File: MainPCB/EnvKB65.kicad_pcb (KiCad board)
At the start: 2 copper layers, 320.8 x 99.3 mm, 151 parts, among them U0 Pico

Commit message: moved mount hole "H5" to the right by 40.5mm on all PCBs
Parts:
- moved H5 40.5 mm to (251.1, 183.5)

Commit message: replaced all mount holes with versions that have pads
I did this because the pcb can get scraped up if you take it apart a bunch of times to clean it, hopefully this mitigates that.
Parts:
- H0, H1, H2, H3, H4, H5: footprint MountingHole:MountingHole_2.2mm_M2 -> MountingHole:MountingHole_2.2mm_M2_Pad
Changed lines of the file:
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@@
     (add_net row4)
   )
+  (module MountingHole:MountingHole_2.2mm_M2_Pad (layer F.Cu)
+    (at 251.125 183.475)
+    (descr "Mounting Hole 2.2mm, M2")
+    (tags "mounting hole 2.2mm m2")
+    (attr virtual)
+    (fp_text reference H5 (at 0 -3.2) (layer Dwgs.User)
+      (effects (font (size 1 1) (thickness 0.15)))
+    )
+    (fp_text value MountingHole (at 0 3.2) (layer F.Fab)
+      (effects (font (size 1 1) (thickness 0.15)))
+    )
+    (fp_text user %R (at 0.3 0) (layer F.Fab)
+      (effects (font (size 1 1) (thickness 0.15)))
+    )
+    (fp_circle (center 0 0) (end 2.2 0) (layer Cmts.User) (width 0.15))
+    (fp_circle (center 0 0) (end 2.45 0) (layer F.CrtYd) (width 0.05))
+    (pad 1 thru_hole circle (at 0 0) (size 4.4 4.4) (drill 2.2) (layers *.Cu *.Mask))
+  )
+  (module MountingHole:MountingHole_2.2mm_M2_Pad (layer F.Cu)
+    (at 224.9 121.6)
+    (descr "Mounting Hole 2.2mm, M2")
+    (tags "mounting hole 2.2mm m2")
+    (attr virtual)
+    (fp_text reference H4 (at 0 -3.2) (layer Dwgs.User)
+      (effects (font (size 1 1) (thickness 0.15)))
+    )
+    (fp_text value MountingHole (at 0 3.2) (layer F.Fab)
+      (effects (font (size 1 1) (thickness 0.15)))
+    )
+    (fp_text user %R (at 0.3 0) (layer F.Fab)
+      (effects (font (size 1 1) (thickness 0.15)))
+    )
+    (fp_circle (center 0 0) (end 2.2 0) (layer Cmts.User) (width 0.15))
+    (fp_circle (center 0 0) (end 2.45 0) (layer F.CrtYd) (width 0.05))
+    (pad 1 thru_hole circle (at 0 0) (size 4.4 4.4) (drill 2.2) (layers *.Cu *.Mask))
+  )
+  (module MountingHole:MountingHole_2.2mm_M2_Pad (layer F.Cu)
+    (at 367.8 178.2)
+    (descr "Mounting Hole 2.2mm, M2")
+    (tags "mounting hole 2.2mm m2")
+    (attr virtual)
+    (fp_text reference H3 (at 0 -3.2) (layer Dwgs.User)
+      (effects (font (size 1 1) (thickness 0.15)))
+    )
+    (fp_text value MountingHole (at 0 3.2) (layer F.Fab)
+      (effects (font (size 1 1) (thickness 0.15)))
+    )
+    (fp_text user %R (at 0.3 0) (layer F.Fab)
+      (effects (font (size 1 1) (thickness 0.15)))
+    )
+    (fp_circle (center 0 0) (end 2.2 0) (layer Cmts.User) (width 0.15))
+    (fp_circle (center 0 0) (end 2.45 0) (layer F.CrtYd) (width 0.05))
+    (pad 1 thru_hole circle (at 0 0) (size 4.4 4.4) (drill 2.2) (layers *.Cu *.Mask))
+  )
+  (module MountingHole:MountingHole_2.2mm_M2_Pad (layer F.Cu)
+    (at 86.8 185.22)
+    (descr "Mounting Hole 2.2mm, M2")
+    (tags "mounting hole 2.2mm m2")
+    (attr virtual)
+    (fp_text reference H2 (at 0 -3.2) (layer Dwgs.User)
+      (effects (font (size 1 1) (thickness 0.15)))
+    )
+    (fp_text value MountingHole (at 0 3.2) (layer F.Fab)
+      (effects (font (size 1 1) (thickness 0.15)))
+    )
+    (fp_text user %R (at 0.3 0) (layer F.Fab)
+      (effects (font (size 1 1) (thickness 0.15)))
+    )
+    (fp_circle (center 0 0) (end 2.2 0) (layer Cmts.User) (width 0.15))
+    (fp_circle (center 0 0) (end 2.45 0) (layer F.CrtYd) (width 0.05))
+    (pad 1 thru_hole circle (at 0 0) (size 4.4 4.4) (drill 2.2) (layers *.Cu *.Mask))
+  )
+  (module MountingHole:MountingHole_2.2mm_M2_Pad (layer F.Cu)
+    (at 69 101)
+    (descr "Mounting Hole 2.2mm, M2")
+    (tags "mounting hole 2.2mm m2")
+    (attr virtual)
+    (fp_text reference H1 (at 0 -3.2) (layer Dwgs.User)
+      (effects (font (size 1 1) (thickness 0.15)))
+    )
+    (fp_text value MountingHole (at 0 3.2) (layer F.Fab)
+      (effects (font (size 1 1) (thickness 0.15)))
+    )
+    (fp_text user %R (at 0.3 0) (layer F.Fab)
+      (effects (font (size 1 1) (thickness 0.15)))
+    )
+    (fp_circle (center 0 0) (end 2.2 0) (layer Cmts.User) (width 0.15))
+    (fp_circle (center 0 0) (end 2.45 0) (layer F.CrtYd) (width 0.05))
+    (pad 1 thru_hole circle (at 0 0) (size 4.4 4.4) (drill 2.2) (layers *.Cu *.Mask))
+  )
+  (module MountingHole:MountingHole_2.2mm_M2_Pad (layer F.Cu)
+    (at 382.2 101)
+    (descr "Mounting Hole 2.2mm, M2")
+    (tags "mounting hole 2.2mm m2")
+    (attr virtual)
+    (fp_text reference H0 (at 0 -3.2) (layer Dwgs.User)
+      (effects (font (size 1 1) (thickness 0.15)))
+    )
+    (fp_text value MountingHole (at 0 3.2) (layer F.Fab)
+      (effects (font (size 1 1) (thickness 0.15)))
+    )
+    (fp_text user %R (at 0.3 0) (layer F.Fab)
+      (effects (font (size 1 1) (thickness 0.15)))
+    )
+    (fp_circle (center 0 0) (end 2.2 0) (layer Cmts.User) (width 0.15))
+    (fp_circle (center 0 0) (end 2.45 0) (layer F.CrtYd) (width 0.05))
+    (pad 1 thru_hole circle (at 0 0) (size 4.4 4.4) (drill 2.2) (layers *.Cu *.Mask))
+  )
   (module MX_Only:MXOnly-2.25U-NoLED (layer F.Cu)
     (at 84.415 168.659)
@@
     )
   )
-  (module MountingHole:MountingHole_2.2mm_M2 (layer F.Cu)
-    (at 251.125 183.475)
-    (descr "Mounting Hole 2.2mm, no annular, M2")
-    (tags "mounting hole 2.2mm no annular m2")
-    (attr virtual)
-    (fp_text reference H5 (at 0 -3.2) (layer Dwgs.User)
-      (effects (font (size 1 1) (thickness 0.15)))
-    )
-    (fp_text value MountingHole (at 0 3.2) (layer F.Fab)
-      (effects (font (size 1 1) (thickness 0.15)))
-    )
-    (fp_circle (center 0 0) (end 2.45 0) (layer F.CrtYd) (width 0.05))
-    (fp_circle (center 0 0) (end 2.2 0) (layer Cmts.User) (width 0.15))
-    (fp_text user %R (at 0.3 0) (layer F.Fab)
-      (effects (font (size 1 1) (thickness 0.15)))
-    )
-    (pad 1 np_thru_hole circle (at 0 0) (size 2.2 2.2) (drill 2.2) (layers *.Cu *.Mask))
-  )
-  (module MountingHole:MountingHole_2.2mm_M2 (layer F.Cu)
-    (at 224.9 121.6)
-    (descr "Mounting Hole 2.2mm, no annular, M2")
-    (tags "mounting hole 2.2mm no annular m2")
-    (attr virtual)
-    (fp_text reference H4 (at 0 -3.2) (layer Dwgs.User)
-      (effects (font (size 1 1) (thickness 0.15)))
-    )
-    (fp_text value MountingHole (at 0 3.2) (layer F.Fab)
-      (effects (font (size 1 1) (thickness 0.15)))
-    )
-    (fp_circle (center 0 0) (end 2.45 0) (layer F.CrtYd) (width 0.05))
-    (fp_circle (center 0 0) (end 2.2 0) (layer Cmts.User) (width 0.15))
-    (fp_text user %R (at 0.225 -0.25) (layer F.Fab)
-      (effects (font (size 1 1) (thickness 0.15)))
-    )
-    (pad 1 np_thru_hole circle (at 0 0) (size 2.2 2.2) (drill 2.2) (layers *.Cu *.Mask))
-  )
-  (module MountingHole:MountingHole_2.2mm_M2 (layer F.Cu)
-    (at 367.8 178.2)
-    (descr "Mounting Hole 2.2mm, no annular, M2")
-    (tags "mounting hole 2.2mm no annular m2")
-    (attr virtual)
-    (fp_text reference H3 (at 0 -3.2 180) (layer Dwgs.User)
-      (effects (font (size 1 1) (thickness 0.15)))
-    )
-    (fp_text value MountingHole (at 0 3.2) (layer F.Fab)
-      (effects (font (size 1 1) (thickness 0.15)))
-    )
-    (fp_circle (center 0 0) (end 2.45 0) (layer F.CrtYd) (width 0.05))
-    (fp_circle (center 0 0) (end 2.2 0) (layer Cmts.User) (width 0.15))
-    (fp_text user %R (at 0.3 0) (layer F.Fab)
-      (effects (font (size 1 1) (thickness 0.15)))
-    )
-    (pad 1 np_thru_hole circle (at 0 0) (size 2.2 2.2) (drill 2.2) (layers *.Cu *.Mask))
-  )
-  (module MountingHole:MountingHole_2.2mm_M2 (layer F.Cu)
-    (at 86.8 185.22)
-    (descr "Mounting Hole 2.2mm, no annular, M2")
-    (tags "mounting hole 2.2mm no annular m2")
-    (attr virtual)
-    (fp_text reference H2 (at 0 -3.2) (layer Dwgs.User)
-      (effects (font (size 1 1) (thickness 0.15)))
-    )
-    (fp_text value MountingHole (at 0 3.2) (layer F.Fab)
-      (effects (font (size 1 1) (thickness 0.15)))
-    )
-    (fp_circle (center 0 0) (end 2.45 0) (layer F.CrtYd) (width 0.05))
-    (fp_circle (center 0 0) (end 2.2 0) (layer Cmts.User) (width 0.15))
-    (fp_text user %R (at 0.3 0) (layer F.Fab)
-      (effects (font (size 1 1) (thickness 0.15)))
-    )
-    (pad 1 np_thru_hole circle (at 0 0) (size 2.2 2.2) (drill 2.2) (layers *.Cu *.Mask))
-  )
-  (module MountingHole:MountingHole_2.2mm_M2 (layer F.Cu)
-    (at 69 101)
-    (descr "Mounting Hole 2.2mm, no annular, M2")
-    (tags "mounting hole 2.2mm no annular m2")
-    (attr virtual)
-    (fp_text reference H1 (at 0 -3.2) (layer Dwgs.User)
-      (effects (font (size 1 1) (thickness 0.15)))
-    )
-    (fp_text value MountingHole (at 0 3.2) (layer F.Fab)
-      (effects (font (size 1 1) (thickness 0.15)))
-    )
-    (fp_circle (center 0 0) (end 2.45 0) (layer F.CrtYd) (width 0.05))
-    (fp_circle (center 0 0) (end 2.2 0) (layer Cmts.User) (width 0.15))
-    (fp_text user %R (at 0.3 0) (layer F.Fab)
-      (effects (font (size 1 1) (thickness 0.15)))
-    )
-    (pad 1 np_thru_hole circle (at 0 0) (size 2.2 2.2) (drill 2.2) (layers *.Cu *.Mask))
-  )
-  (module MountingHole:MountingHole_2.2mm_M2 (layer F.Cu)
-    (at 382.2 101)
-    (descr "Mounting Hole 2.2mm, no annular, M2")
-    (tags "mounting hole 2.2mm no annular m2")
-    (attr virtual)
-    (fp_text reference H0 (at 0 -3.2) (layer Dwgs.User) hide
-      (effects (font (size 1 1) (thickness 0.15)))
-    )
-    (fp_text value MountingHole (at 0 3.2) (layer F.Fab)
-      (effects (font (size 1 1) (thickness 0.15)))
-    )
-    (fp_circle (center 0 0) (end 2.45 0) (layer F.CrtYd) (width 0.05))
-    (fp_circle (center 0 0) (end 2.2 0) (layer Cmts.User) (width 0.15))
-    (fp_text user %R (at 0.3 0) (layer F.Fab)
-      (effects (font (size 1 1) (thickness 0.15)))
-    )
-    (pad 1 np_thru_hole circle (at 0 0) (size 2.2 2.2) (drill 2.2) (layers *.Cu *.Mask))
-  )
   (module MCU_RaspberryPi_and_Boards:RPi_Pico_SMD_TH (layer F.Cu)

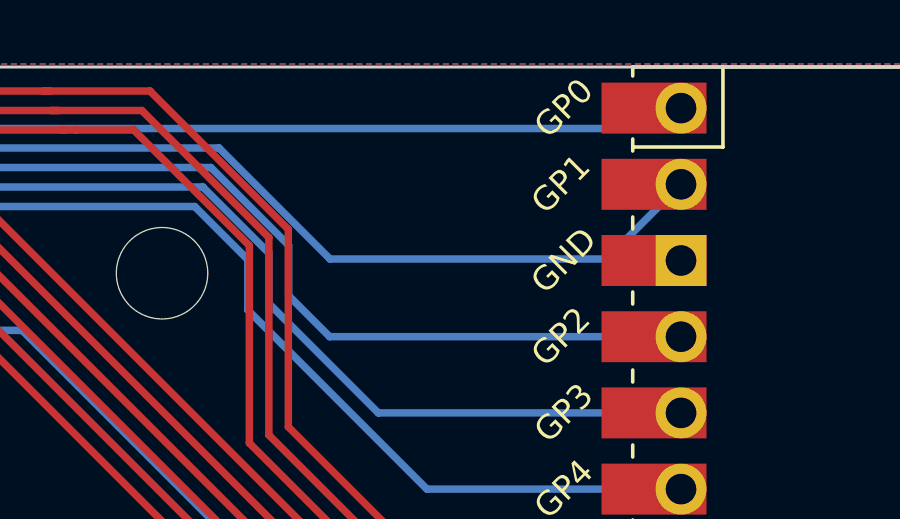
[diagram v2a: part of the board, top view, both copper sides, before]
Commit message: changed my mind, I wanted the 32u version to have more switches, going to figure out if I can fit the MCU somewhere on the back of the board.
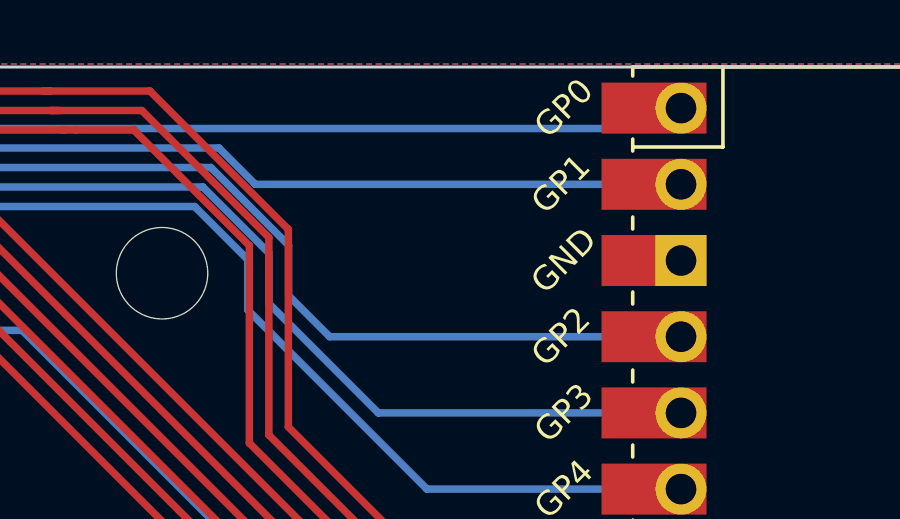
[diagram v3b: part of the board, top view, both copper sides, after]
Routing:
- net col1: track 356.4 -> 354.4 mm

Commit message: See List
* removed RP2040 and atmega32u4 versions
* updated main PCB to have larger holes
* fixed some stuff on the main PCB and added some labels
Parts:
- H0, H1, H2, H3, H4, H5: footprint MountingHole:MountingHole_2.2mm_M2_Pad -> MountingHole:MountingHole_4.3mm_M4
- moved D_58 2.91 mm to (88.0, 191.4), turned to 180 degrees
- moved D_63 0.90 mm to (251.9, 191.1)
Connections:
- net Net-(U0-Pad29) renamed GPIO22
- net Net-(U0-Pad31) renamed GPIO26
- net Net-(U0-Pad32) renamed GPIO27
- net Net-(U0-Pad34) renamed GPIO28
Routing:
- net col13: track 154.3 -> 141.4 mm
- net col7: track 244.2 -> 236.5 mm
- net col12: track 181.8 -> 174.9 mm
- net col8: track 243.2 -> 237.6 mm
- net col9: track 205.8 -> 200.8 mm
- net col6: track 280.2 -> 275.2 mm
- net col5: track 277.4 -> 272.5 mm
- net col10: track 211.1 -> 206.6 mm
- net col11: track 192.1 -> 187.9 mm
- net Net-(D_58-Pad2): track 10.4 -> 14.3 mm
- net row4: track 351.9 -> 348.7 mm
- net Net-(D_63-Pad2): track 19.9 -> 20.5 mm
- net col14: vias 0 -> 1
- net gnd: vias 0 -> 2
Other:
- board text added: "A Raspberry Pi Pico or compatible alternative can be installed here"
- board text added: "GP22, GP26, GP27 and GP28 are spare."
